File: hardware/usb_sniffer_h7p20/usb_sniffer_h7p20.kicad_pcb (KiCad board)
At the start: 4 copper layers, 47.5 x 47.5 mm, 140 parts, among them J1 FPGA_JTAG, J2 USB_C_Receptacle_USB2.0_16P, J3 USB_A, J4 USB_C_Receptacle_USB2.0_16P, J5 FFC-40P-0.5mm,NC, J6 Trigger, U1 H7P20N0L128-M3H1, U11 EA3036C, U2 LM2903A-VR, U3 LM2903A-VR, U4 LM2903A-VR, U5 USB3343, U6 P25Q64SH-SSH-IR, U7 CY7C68013A-56LTX, U8 24C32, U9 CJ3439KDW, Y2 24M

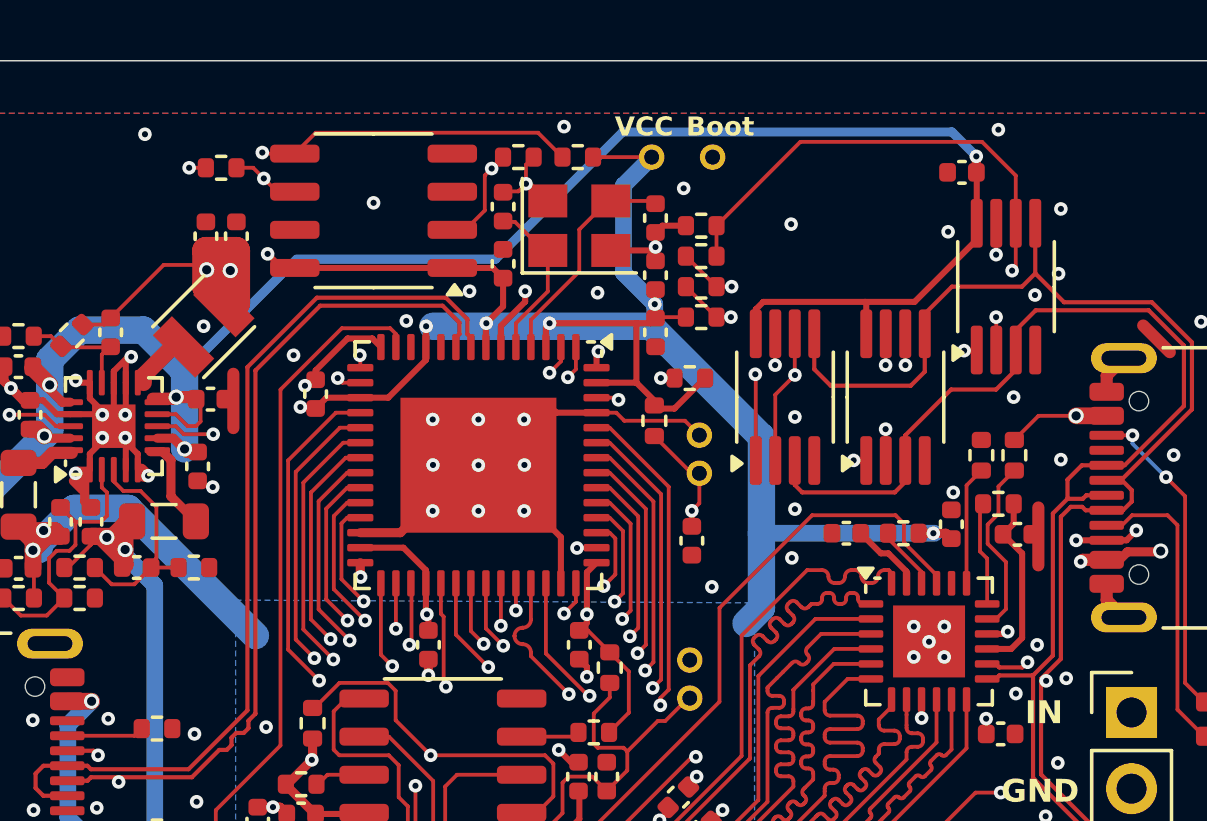
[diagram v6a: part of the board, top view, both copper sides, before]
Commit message: [usb_sniffer_h7p20] 换GSV332-MR，待测试
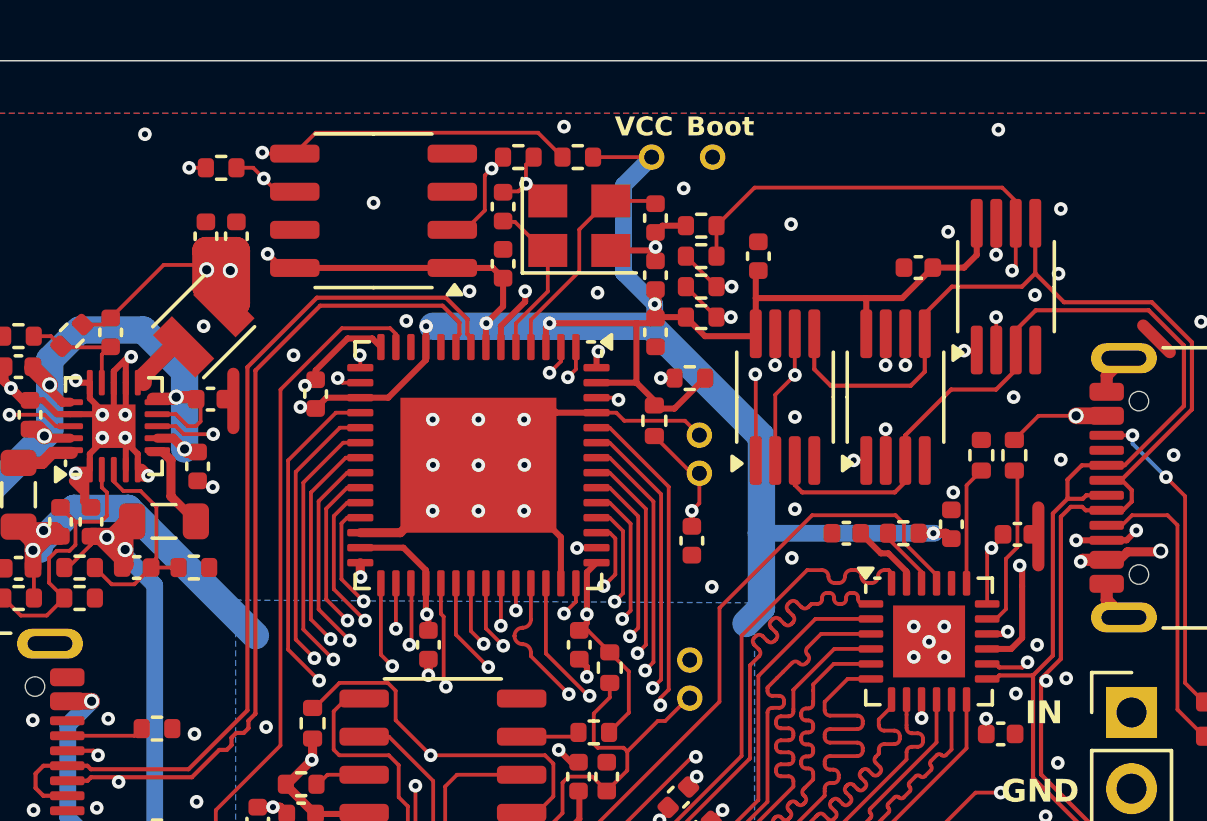
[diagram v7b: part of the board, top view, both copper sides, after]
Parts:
- removed R1: 0, Resistor_SMD:R_0402_1005Metric
- added C1: 0.1uF, Capacitor_SMD:C_0402_1005Metric, F.Cu at (117.0, 80.3)
- U2, U3, U4: value LM2903A-VR -> GSV332-MR
- moved C3 3.49 mm to (122.3, 80.6)
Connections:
- C10 pad 2: Net-(U5-VDD33) -> Net-(U5-ID)
- C3 pad 2: /VCC_5V -> /VCC_3V3
- U2 pad 8: /VCC_5V -> /VCC_3V3
- U3 pad 8: /VCC_5V -> /VCC_3V3
- U4 pad 8: /VCC_5V -> /VCC_3V3
- U5 pad 15: Net-(U5-VDD33) -> Net-(U5-ID)
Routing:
- net /VCC_5V: track 143.7 -> 100.6 mm, vias 10 -> 9
- net /VCC_3V3: track 187.9 -> 203.1 mm
- net Net-(U5-VDD33): track 6.20 -> 0.00 mm
- net Net-(U5-ID): track 3.48 -> 7.49 mm, vias 0 -> 2
- net /USB334x/CMP_REF_1: track 18.7 -> 16.9 mm
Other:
- board text added: "USB Sniffer H7P20 20250824"
- board text removed: "USB Sniffer H7P20 20250818"
